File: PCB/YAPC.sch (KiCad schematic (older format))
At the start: 0 parts

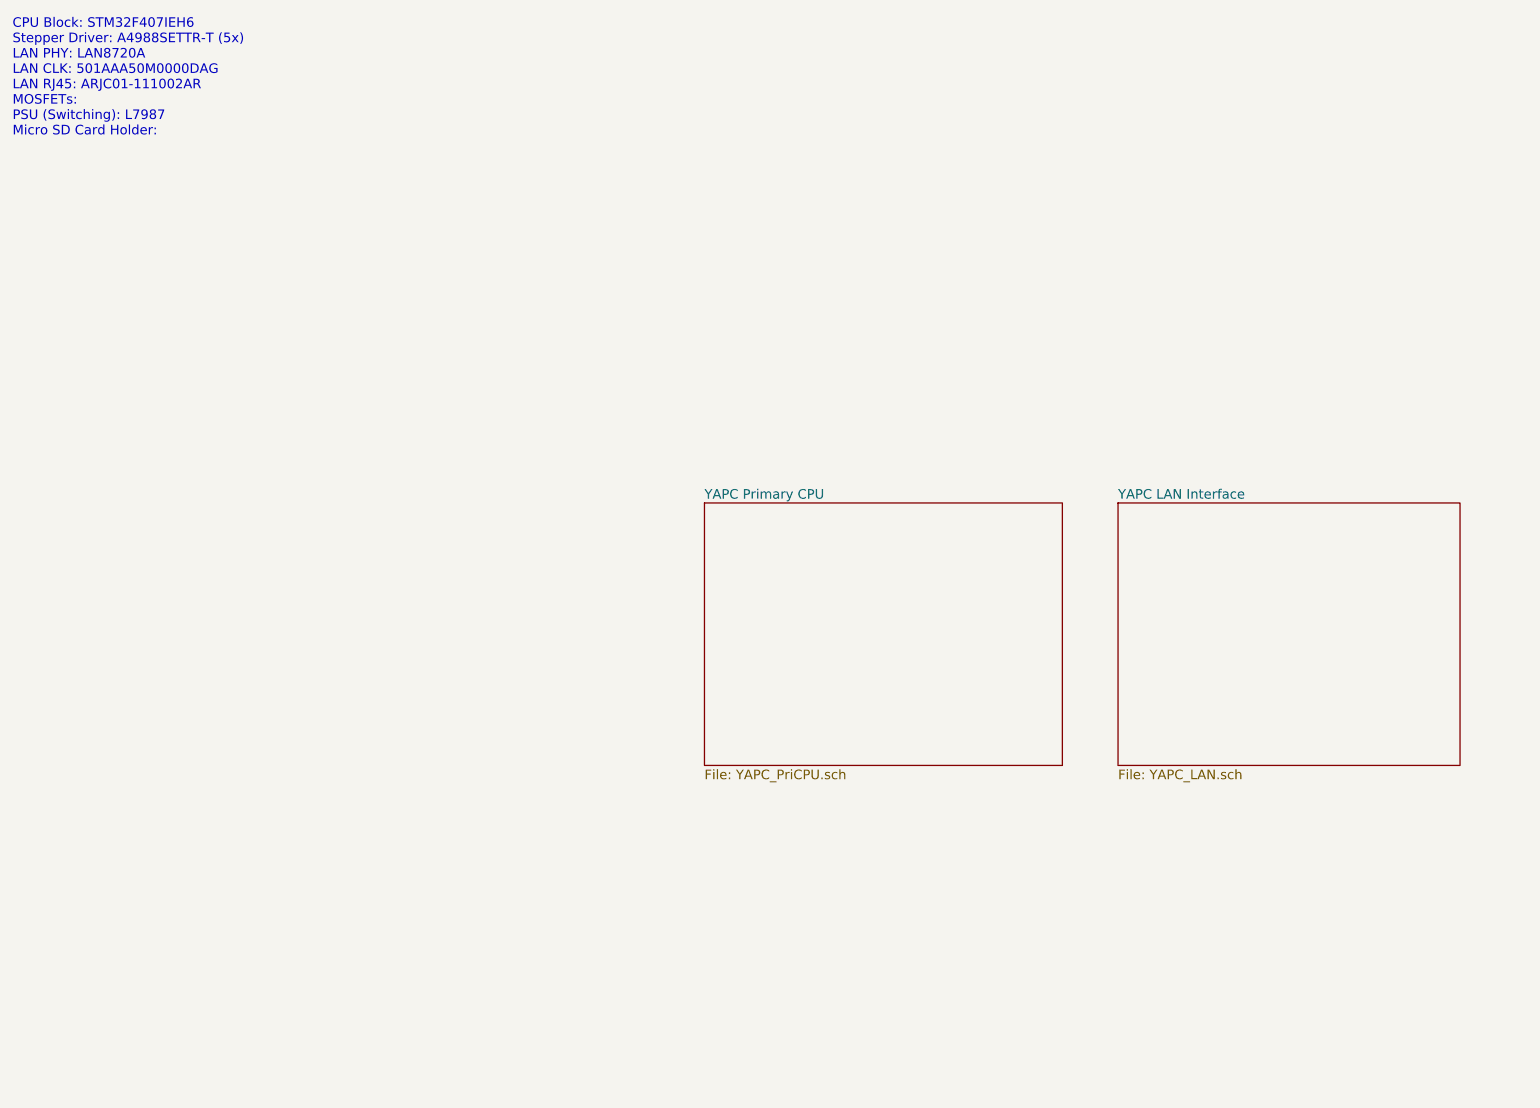
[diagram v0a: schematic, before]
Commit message: Create sheet hierarchy
Add more sheets into the project, ready for the various components to be
added
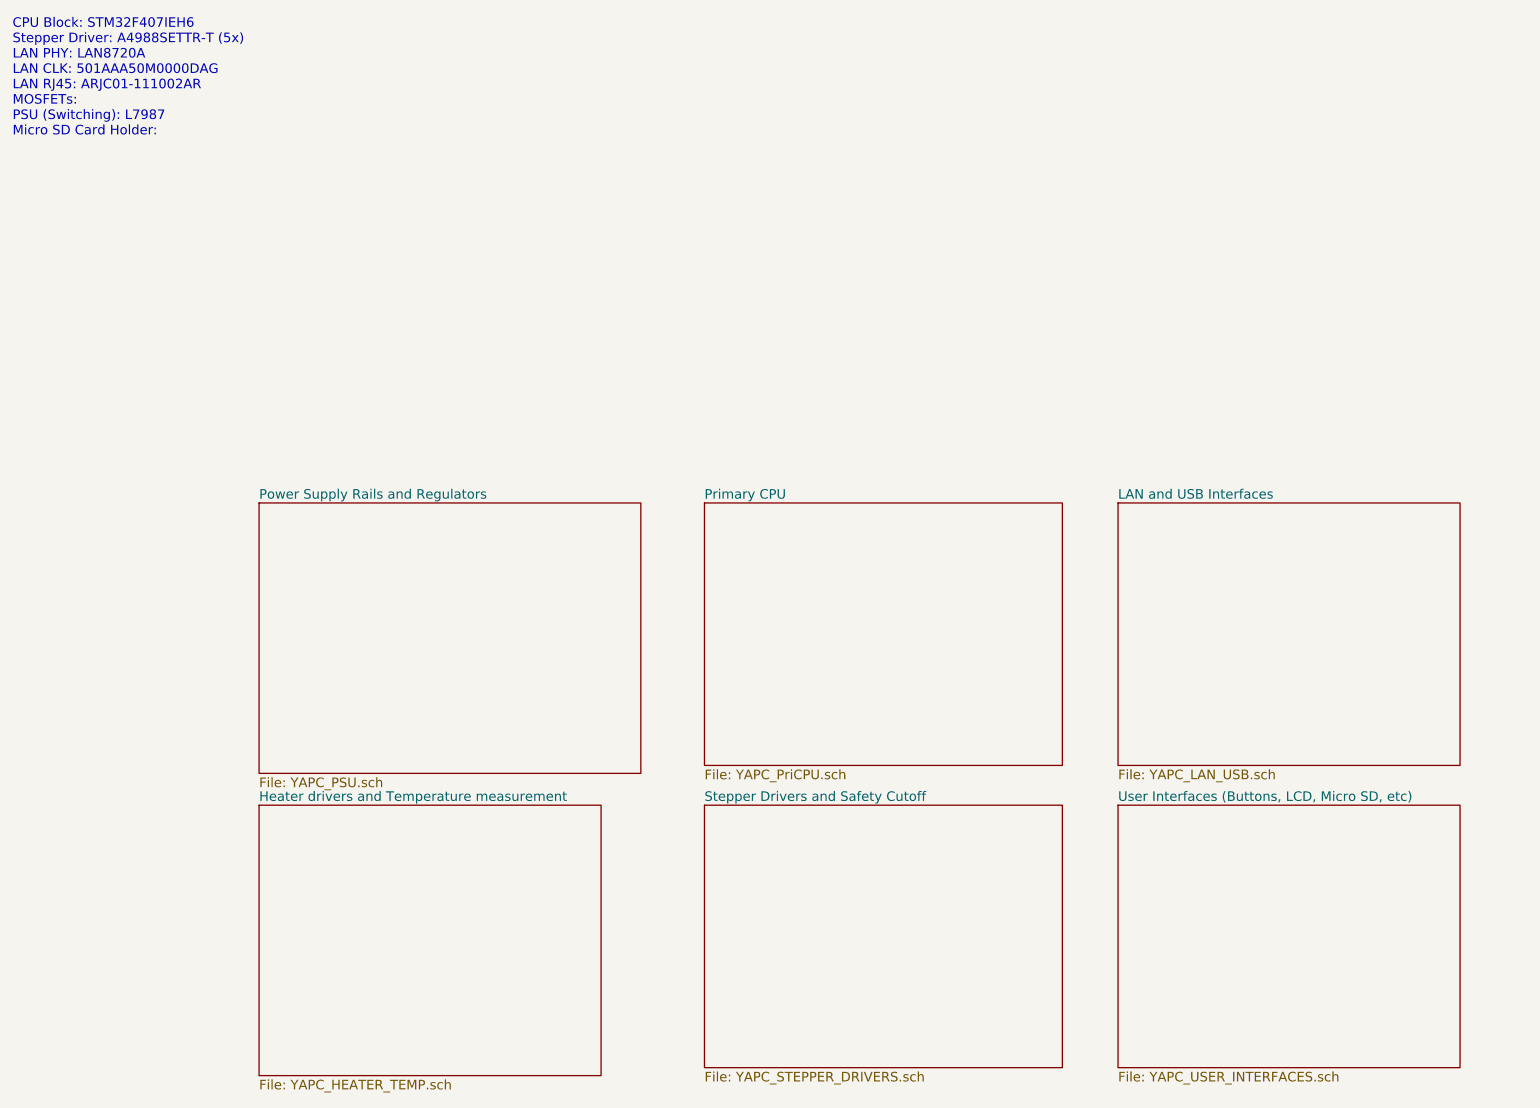
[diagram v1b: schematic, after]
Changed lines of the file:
@@
 $Descr A3 16535 11693
 encoding utf-8
-Sheet 1 3
+Sheet 1 6
 Title "Yet Another Printer Controller"
 Date ""
@@
 S 9400 5900 2250 1650
 U 55B5AEC5
-F0 "YAPC Primary CPU" 60
+F0 "Primary CPU" 60
 F1 "YAPC_PriCPU.sch" 60
 $EndSheet
@@
 S 12000 5900 2150 1650
 U 55BDA0EC
-F0 "YAPC LAN Interface" 60
-F1 "YAPC_LAN.sch" 60
+F0 "LAN and USB Interfaces" 60
+F1 "YAPC_LAN_USB.sch" 60
+$EndSheet
+$Sheet
+S 12000 7800 2150 1650
+U 56AFC97A
+F0 "User Interfaces (Buttons, LCD, Micro SD, etc)" 60
+F1 "YAPC_USER_INTERFACES.sch" 60
+$EndSheet
+$Sheet
+S 9400 7800 2250 1650
+U 56AFC9A7
+F0 "Stepper Drivers and Safety Cutoff" 60
+F1 "YAPC_STEPPER_DRIVERS.sch" 60
+$EndSheet
+$Sheet
+S 6600 7800 2150 1700
+U 56AFC9F3
+F0 "Heater drivers and Temperature measurement" 60
+F1 "YAPC_HEATER_TEMP.sch" 60
+$EndSheet
+$Sheet
+S 6600 5900 2400 1700
+U 56AFCC20
+F0 "Power Supply Rails and Regulators" 60
+F1 "YAPC_PSU.sch" 60
 $EndSheet
 $EndSCHEMATC
